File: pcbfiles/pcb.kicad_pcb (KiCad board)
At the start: 2 copper layers, 269.9 x 139.7 mm, 256 parts, among them J1 Conn_01x06, J2 Conn_01x06, J3 Conn_01x06, J4 Conn_01x06, J5 Conn_01x04_Female, J6 Conn_01x04_Female, Q1 AO3401A, Q2 AO3401A, SW1 SW_SPST, SW10 SW_SPST, SW11 SW_SPST, SW12 SW_SPST, SW13 SW_SPST, SW14 SW_SPST, SW15 SW_SPST, SW16 SW_SPST, SW17 SW_SPST, SW18 SW_SPST, SW19 SW_SPST, SW2 SW_SPST, SW20 SW_SPST, SW21 SW_SPST, SW22 SW_SPST, SW23 SW_SPST, SW24 SW_SPST, SW25 SW_SPST, SW26 SW_SPST, SW27 SW_SPST, SW28 SW_SPST, SW29 SW_SPST, SW3 SW_SPST, SW30 SW_SPST, SW31 SW_SPST, SW32 SW_SPST, SW33 SW_SPST, SW34 SW_SPST, SW35 SW_SPST, SW36 SW_SPST, SW37 SW_SPST, SW38 SW_SPST, SW39 SW_SPST, SW4 SW_SPST, SW40 SW_SPST, SW41 SW_SPST, SW42 SW_SPST, SW43 SW_SPST, SW44 SW_SPST, SW45 SW_SPST, SW46 SW_SPST, SW47 SW_SPST, SW48 SW_SPST, SW49 SW_SPST, SW5 SW_SPST, SW50 SW_SPST, SW51 SW_SPST, SW52 SW_SPST, SW53 SW_SPST, SW54 SW_SPST, SW55 SW_SPST, SW56 SW_SPST, SW57 SW_SPST, SW58 SW_SPST, SW59 SW_SPST, SW6 SW_SPST, SW60 SW_SPST, SW61 SW_SPST, SW62 SW_SPST, SW63 SW_SPST, SW64 SW_SPST, SW65 SW_SPST, SW66 SW_SPST, SW67 SW_SPST, SW68 SW_SPST, SW69 SW_SPST, SW7 SW_SPST, SW70 SW_SPST, SW71 SW_SPST, SW72 SW_SPST, SW73 SW_SPST, SW74 SW_SPST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

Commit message: Incremental routing
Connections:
- U5 pad 13: unconnected-(U5-Pad13) -> LH_ROW3
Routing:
- net VBUS: track 14.6 -> 65.3 mm, vias 0 -> 2
- net DBA_P2: track 10.9 -> 42.8 mm
- net LH_ROW2: track 124.9 -> 148.4 mm, vias 0 -> 2
- net VDD_NRF: track 2.25 -> 15.1 mm
- net RESET: track 0.00 -> 6.55 mm
- net LH_ROW3: track 107.4 -> 111.9 mm
- net DBA_P1: track 44.8 -> 42.7 mm
- net DBA_P5: track 44.7 -> 43.3 mm
- net unconnected-(U5-Pad4): track 1.10 -> 0.00 mm
- net unconnected-(U5-Pad3): track 1.10 -> 0.00 mm
- net unconnected-(U5-Pad2): track 1.10 -> 0.00 mm
- net DBA_P4: track 43.9 -> 43.2 mm
- net LH_COL0: vias 5 -> 7

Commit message: routing
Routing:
- net D-: track 5.70 -> 84.9 mm
- net D+: track 12.1 -> 82.8 mm
- net VBUS: track 65.3 -> 56.9 mm
- net LH_ROW2: vias 2 -> 4
- net LH_ROW3: vias 0 -> 2

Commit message: routing
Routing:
- net D+: track 82.8 -> 126.8 mm
- net VBUS: track 56.9 -> 16.0 mm, vias 2 -> 1
- net D-: track 84.9 -> 125.6 mm
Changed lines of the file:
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@@
   (arc (start 160.115395 69.557107) (mid 159.790972 69.77388) (end 159.408288 69.85) (width 0.25) (layer "B.Cu") (net 8))
   (arc (start 158.526714 69.85) (mid 158.144031 69.92612) (end 157.819607 70.142893) (width 0.25) (layer "B.Cu") (net 8))
-  (segment (start 7.9375 66.05) (end 7.9375 26.9875) (width 0.35) (layer "F.Cu") (net 9))
-  (via (at 7.9375 66.05) (size 0.8) (drill 0.4) (layers "F.Cu" "B.Cu") (net 9))
   (via (at 7.9375 26.9875) (size 0.8) (drill 0.4) (layers "F.Cu" "B.Cu") (net 9))
   (segment (start 79.375 68.675) (end 79.375 69.8) (width 0.35) (layer "B.Cu") (net 9))
@@
   (segment (start 7.9375 25.5875) (end 7.9375 26.9875) (width 0.35) (layer "B.Cu") (net 9))
   (segment (start 83.39375 67.675) (end 85.579536 67.675) (width 0.35) (layer "B.Cu") (net 9))
-  (segment (start 9.75 66.05) (end 7.9375 66.05) (width 0.35) (layer "B.Cu") (net 9))
   (segment (start 10.31875 26.075) (end 8.425 26.075) (width 0.35) (layer "B.Cu") (net 9))
   (arc (start 79.375 68.675) (mid 79.667893 67.967893) (end 80.375 67.675) (width 0.35) (layer "B.Cu") (net 9))
@@
   (arc (start -2.972895 29.592893) (mid -2.648472 29.37612) (end -2.265788 29.3) (width 0.35) (layer "B.Cu") (net 47))
   (arc (start -3.028554 33.851448) (mid -3.190766 33.743062) (end -3.382107 33.705002) (width 0.35) (layer "B.Cu") (net 47))
-  (segment (start 1.08125 31) (end 1.43125 30.65) (width 0.2) (layer "B.Cu") (net 48))
-  (segment (start 1.43125 30.65) (end 1.43125 30.75) (width 0.2) (layer "B.Cu") (net 48))
+  (segment (start 46.4 31.75) (end 2.43125 31.75) (width 0.2) (layer "B.Cu") (net 48))
+  (segment (start 1.091249 31.000001) (end 1.441249 30.650001) (width 0.2) (layer "B.Cu") (net 48))
   (segment (start 45.75 68.25) (end 9.75 68.25) (width 0.2) (layer "B.Cu") (net 48))
-  (segment (start -2.5 32) (end -1.33 32) (width 0.2) (layer "B.Cu") (net 48))
+  (segment (start -2.990001 31.500001) (end -2.990001 31.500001) (width 0.2) (layer "B.Cu") (net 48))
+  (segment (start 1.441249 30.650001) (end 1.441249 30.750001) (width 0.2) (layer "B.Cu") (net 48))
+  (segment (start -2.490001 31.000001) (end -1.320001 31.000001) (width 0.2) (layer "B.Cu") (net 48))
   (segment (start 47.85 33.2) (end 47.85 66.15) (width 0.2) (layer "B.Cu") (net 48))
-  (segment (start -1.33 31) (end 1.08125 31) (width 0.2) (layer "B.Cu") (net 48))
-  (segment (start -3 31.5) (end -3 31.5) (width 0.2) (layer "B.Cu") (net 48))
-  (segment (start -2.5 31) (end -1.33 31) (width 0.2) (layer "B.Cu") (net 48))
-  (arc (start -2.5 31) (mid -2.853553 31.146447) (end -3 31.5) (width 0.2) (layer "B.Cu") (net 48))
+  (segment (start -2.490001 32.000001) (end -1.320001 32.000001) (width 0.2) (layer "B.Cu") (net 48))
+  (segment (start -1.320001 31.000001) (end 1.091249 31.000001) (width 0.2) (layer "B.Cu") (net 48))
   (arc (start 1.43125 30.75) (mid 1.724143 31.457107) (end 2.43125 31.75) (width 0.2) (layer "B.Cu") (net 48))
+  (arc (start -2.490001 32.000001) (mid -2.843554 31.853554) (end -2.990001 31.500001) (width 0.2) (layer "B.Cu") (net 48))
   (arc (start 45.75 68.25) (mid 47.234924 67.634924) (end 47.85 66.15) (width 0.2) (layer "B.Cu") (net 48))
-  (arc (start -2.5 32) (mid -2.853553 31.853553) (end -3 31.5) (width 0.2) (layer "B.Cu") (net 48))
+  (arc (start -2.490001 31.000001) (mid -2.843554 31.146448) (end -2.990001 31.500001) (width 0.2) (layer "B.Cu") (net 48))
   (arc (start 46.4 31.75) (mid 47.425305 32.174695) (end 47.85 33.2) (width 0.2) (layer "B.Cu") (net 48))
-  (segment (start -1.33 31.5) (end -0.16 31.5) (width 0.2) (layer "B.Cu") (net 49))
-  (segment (start 9.75 67.15) (end 46.4 67.15) (width 0.2) (layer "B.Cu") (net 49))
+  (segment (start -1.320001 32.500001) (end -0.150001 32.500001) (width 0.2) (layer "B.Cu") (net 49))
+  (segment (start 1.091249 32.500001) (end 0.849999 32.500001) (width 0.2) (layer "B.Cu") (net 49))
+  (segment (start 11.548882 67.698883) (end 11.6 67.698883) (width 0.2) (layer "B.Cu") (net 49))
+  (segment (start 46.4 32.2) (end 4.8 32.2) (width 0.2) (layer "B.Cu") (net 49))
+  (segment (start 1.43125 32.85) (end 1.08125 32.5) (width 0.2) (layer "B.Cu") (net 49))
+  (segment (start 0.349999 32.000001) (end 0.349999 32.000001) (width 0.2) (layer "B.Cu") (net 49))
+  (segment (start 4.3 32.7) (end 4.3 33.35) (width 0.2) (layer "B.Cu") (net 49))
+  (segment (start 1.43125 32.85) (end 1.43125 32.85) (width 0.2) (layer "B.Cu") (net 49))
+  (segment (start 0.349999 32.000001) (end 0.349999 32.000001) (width 0.2) (layer "B.Cu") (net 49))
+  (segment (start 12.148882 67.15) (end 12.2 67.15) (width 0.2) (layer "B.Cu") (net 49))
   (segment (start 3.8 33.85) (end 2.43125 33.85) (width 0.2) (layer "B.Cu") (net 49))
-  (segment (start -1.33 32.5) (end -0.16 32.5) (width 0.2) (layer "B.Cu") (net 49))
-  (segment (start 4.3 33.35) (end 4.3 32.7) (width 0.2) (layer "B.Cu") (net 49))
-  (segment (start 1.43125 32.85) (end 1.08125 32.5) (width 0.2) (layer "B.Cu") (net 49))
-  (segment (start 1.43125 32.85) (end 1.43125 32.85) (width 0.2) (layer "B.Cu") (net 49))
+  (segment (start 11.874441 67.424442) (end 11.874441 67.424441) (width 0.2) (layer "B.Cu") (net 49))
+  (segment (start 12.2 67.15) (end 46.4 67.15) (width 0.2) (layer "B.Cu") (net 49))
+  (segment (start 1.43125 32.85) (end 1.43125 33.18125) (width 0.2) (layer "B.Cu") (net 49))
+  (segment (start 11.274441 67.424441) (end 11.274441 67.424442) (width 0.2) (layer "B.Cu") (net 49))
   (segment (start 47.4 66.15) (end 47.4 33.2) (width 0.2) (layer "B.Cu") (net 49))
-  (segment (start 1.08125 32.5) (end 0.84 32.5) (width 0.2) (layer "B.Cu") (net 49))
-  (segment (start 0.34 32) (end 0.34 32) (width 0.2) (layer "B.Cu") (net 49))
-  (segment (start 4.8 32.2) (end 6.3 32.2) (width 0.2) (layer "B.Cu") (net 49))
-  (segment (start 0.34 32) (end 0.34 32) (width 0.2) (layer "B.Cu") (net 49))
-  (segment (start 1.43125 32.85) (end 1.43125 33.18125) (width 0.2) (layer "B.Cu") (net 49))
-  (arc (start 0.34 32) (mid 0.193553 31.646447) (end -0.16 31.5) (width 0.2) (layer "B.Cu") (net 49))
+  (segment (start 9.75 67.15) (end 11 67.15) (width 0.2) (layer "B.Cu") (net 49))
+  (segment (start -1.320001 31.500001) (end -0.150001 31.500001) (width 0.2) (layer "B.Cu") (net 49))
+  (arc (start -0.150001 32.500001) (mid 0.203552 32.353554) (end 0.349999 32.000001) (width 0.2) (layer "B.Cu") (net 49))
+  (arc (start 2.43125 33.85) (mid 1.724143 33.557107) (end 1.43125 32.85) (width 0.2) (layer "B.Cu") (net 49))
+  (arc (start 11.874441 67.424441) (mid 11.954823 67.230382) (end 12.148882 67.15) (width 0.2) (layer "B.Cu") (net 49))
+  (arc (start 11 67.15) (mid 11.194059 67.230382) (end 11.274441 67.424441) (width 0.2) (layer "B.Cu") (net 49))
+  (arc (start 46.4 67.15) (mid 47.107107 66.857107) (end 47.4 66.15) (width 0.2) (layer "B.Cu") (net 49))
+  (arc (start 0.349999 32.000001) (mid 0.203552 31.646448) (end -0.150001 31.500001) (width 0.2) (layer "B.Cu") (net 49))
+  (arc (start 11.6 67.698883) (mid 11.794059 67.618501) (end 11.874441 67.424442) (width 0.2) (layer "B.Cu") (net 49))
+  (arc (start 4.8 32.2) (mid 4.446447 32.346447) (end 4.3 32.7) (width 0.2) (layer "B.Cu") (net 49))
+  (arc (start 4.3 33.35) (mid 4.153553 33.703553) (end 3.8 33.85) (width 0.2) (layer "B.Cu") (net 49))
   (arc (start 47.4 33.2) (mid 47.107107 32.492893) (end 46.4 32.2) (width 0.2) (layer "B.Cu") (net 49))
-  (arc (start 4.3 32.7) (mid 4.446447 32.346447) (end 4.8 32.2) (width 0.2) (layer "B.Cu") (net 49))
-  (arc (start -0.16 32.5) (mid 0.193553 32.353553) (end 0.34 32) (width 0.2) (layer "B.Cu") (net 49))
-  (arc (start 0.34 32) (mid 0.486447 32.353553) (end 0.84 32.5) (width 0.2) (layer "B.Cu") (net 49))
-  (arc (start 2.43125 33.85) (mid 1.724143 33.557107) (end 1.43125 32.85) (width 0.2) (layer "B.Cu") (net 49))
-  (arc (start 3.8 33.85) (mid 4.153553 33.703553) (end 4.3 33.35) (width 0.2) (layer "B.Cu") (net 49))
-  (arc (start 47.4 66.15) (mid 47.107107 66.857107) (end 46.4 67.15) (width 0.2) (layer "B.Cu") (net 49))
+  (arc (start 0.349999 32.000001) (mid 0.496446 32.353554) (end 0.849999 32.500001) (width 0.2) (layer "B.Cu") (net 49))
+  (arc (start 11.274441 67.424442) (mid 11.354823 67.618501) (end 11.548882 67.698883) (width 0.2) (layer "B.Cu") (net 49))
   (segment (start 246.5705 43.18) (end 246.5705 40.75) (width 0.25) (layer "B.Cu") (net 50))
   (segment (start 249.2375 39.75) (end 247.5705 39.75) (width 0.25) (layer "B.Cu") (net 50))
@@
   (via (at -7.14375 42.06875) (size 0.8) (drill 0.4) (layers "F.Cu" "B.Cu") (net 105))
   (arc (start -4.7625 41.06875) (mid -5.055393 41.775857) (end -5.7625 42.06875) (width 0.25) (layer "F.Cu") (net 105))
+  (segment (start -3.455776 32.707108) (end -3.472687 32.690197) (width 0.25) (layer "B.Cu") (net 105))
   (segment (start -1.33 33) (end -2.758668 33) (width 0.25) (layer "B.Cu") (net 105))
   (segment (start -4.7625 32.54375) (end -3.836239 32.54375) (width 0.25) (layer "B.Cu") (net 105))
-  (segment (start -3.465775 32.707107) (end -3.482686 32.690196) (width 0.25) (layer "B.Cu") (net 105))
   (segment (start -7.14375 43.5375) (end -7.14375 42.06875) (width 0.25) (layer "B.Cu") (net 105))
   (arc (start -2.758668 33) (mid -3.141351 32.92388) (end -3.465775 32.707107) (width 0.25) (layer "B.Cu") (net 105))

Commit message: Today's minor progress
I had a short break from responsibilities today, and made some progress. Discord wants to update and I'm data limited, so I can't message you right now, but I'm happy with my progress and appreciate your flexibility on deadline.
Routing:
- net RESET: track 6.55 -> 112.8 mm, vias 0 -> 2
- net BVOLT: track 2.38 -> 105.1 mm, vias 0 -> 4
- net VDD_NRF: track 15.1 -> 98.3 mm, vias 0 -> 2
- net Net-(D94-Pad1): track 3.98 -> 14.4 mm
- net VBAT: track 24.0 -> 27.7 mm
- net Net-(C5-Pad1): track 12.2 -> 8.79 mm

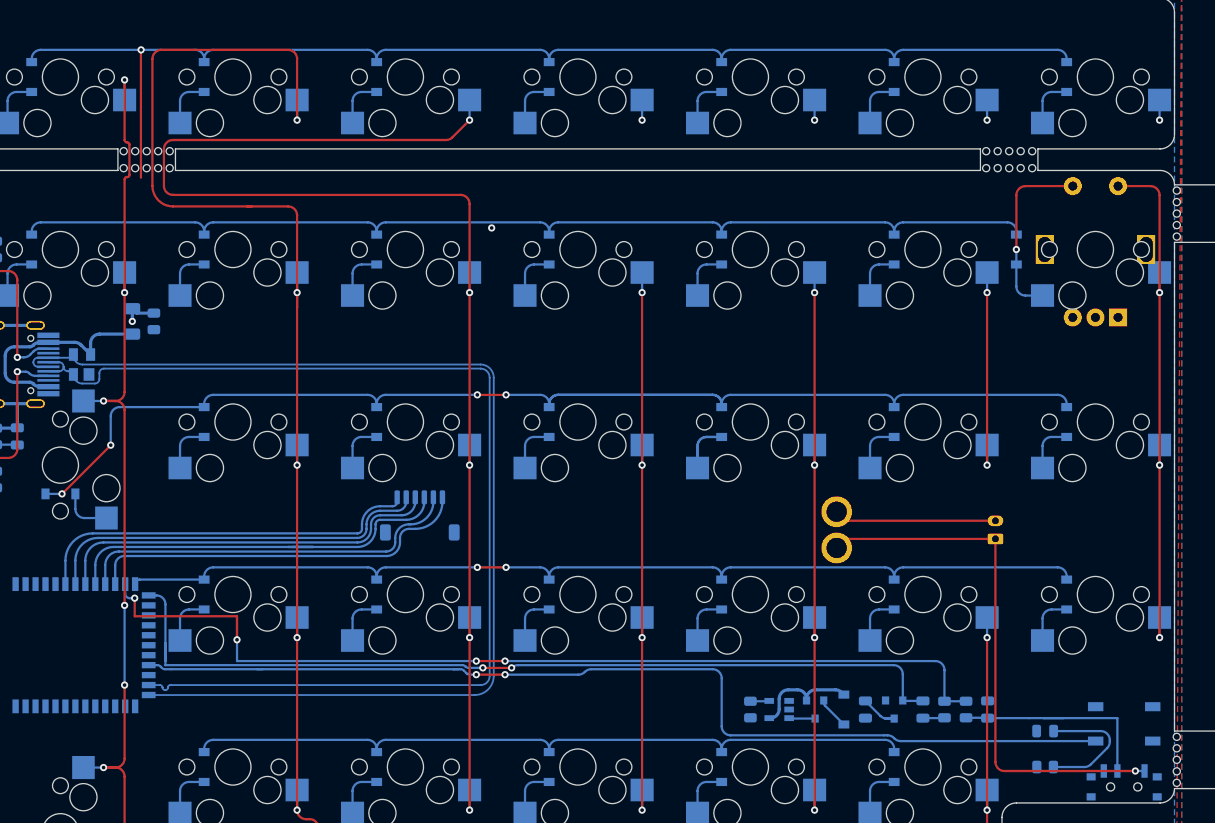
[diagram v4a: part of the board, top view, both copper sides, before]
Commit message: Routing for the left half.
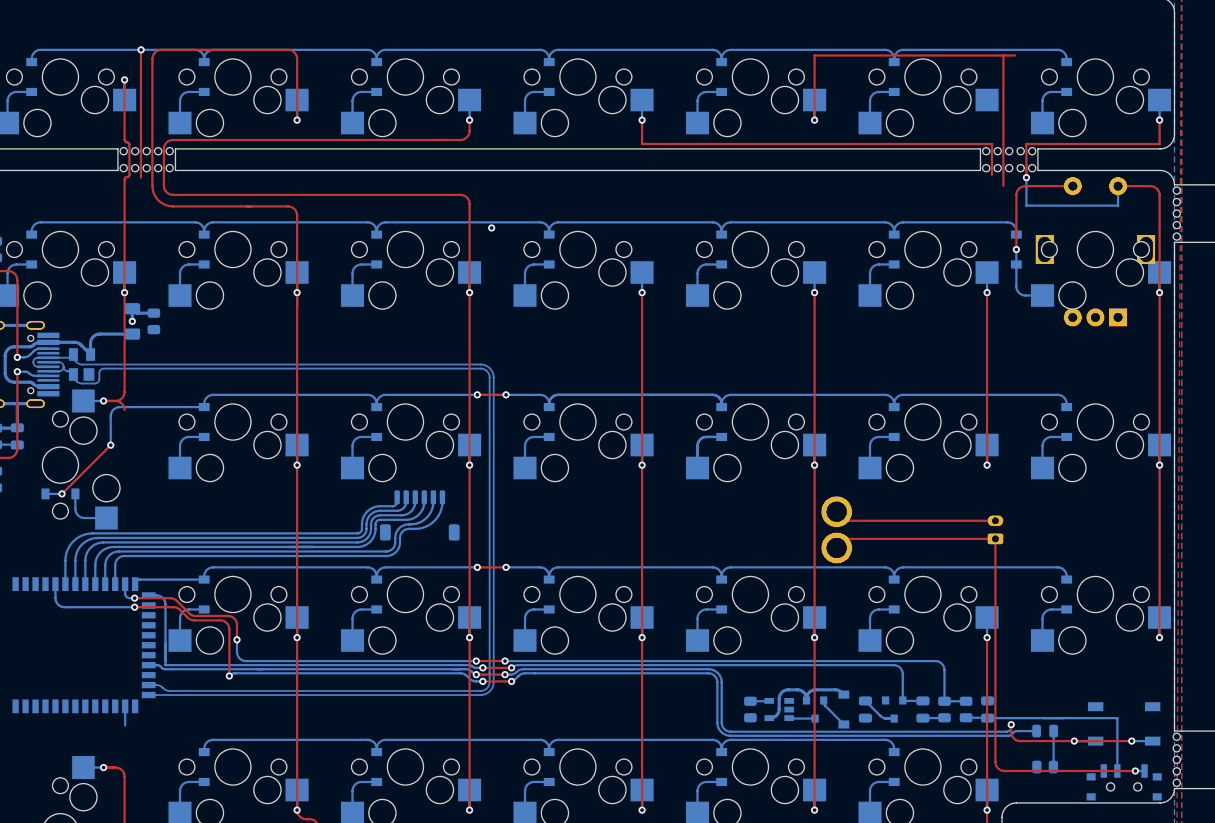
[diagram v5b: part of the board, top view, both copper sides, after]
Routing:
- net LED_1: track 0.00 -> 123.2 mm, vias 0 -> 4
- net LH_COL3: track 68.3 -> 112.9 mm
- net LH_COL4: track 68.3 -> 111.9 mm
- net LH_COL0: track 130.3 -> 90.3 mm, vias 7 -> 5
- net ENC_P1: track 62.9 -> 99.3 mm, vias 4 -> 5
- net Net-(D94-Pad1): track 14.4 -> 3.98 mm
- net RESET: track 112.8 -> 122.9 mm, vias 2 -> 5
- net LH_COL5: track 70.5 -> 68.3 mm, vias 6 -> 5
- net BVOLT: track 105.1 -> 102.9 mm
- net unconnected-(U5-Pad26): track 0.00 -> 2.10 mm
- net LH_COL2: track 152.1 -> 153.9 mm
- net D-: track 125.6 -> 126.2 mm

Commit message: Routing progress.
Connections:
- U5 pad 2: unconnected-(U5-Pad2) -> LH_ROW1
- U5 pad 3: unconnected-(U5-Pad3) -> LH_ROW0
- U5 pad 4: unconnected-(U5-Pad4) -> LH_ROW2
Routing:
- net DBA_P2: track 42.8 -> 154.6 mm, vias 0 -> 2
- net LH_ROW5: track 0.00 -> 91.8 mm
- net DBA_P5: track 43.3 -> 128.8 mm, vias 0 -> 2
- net DBA_P4: track 43.2 -> 118.2 mm, vias 0 -> 2
- net DBA_P3: track 47.9 -> 119.7 mm, vias 0 -> 2
- net DBA_P6: track 43.4 -> 114.9 mm, vias 0 -> 2
- net DBA_P1: track 42.7 -> 110.0 mm, vias 0 -> 2
- net LH_ROW0: track 139.0 -> 193.5 mm, vias 1 -> 2
- net unconnected-(U5-Pad30): track 0.00 -> 53.4 mm
- net LH_COL0: track 90.3 -> 140.2 mm, vias 5 -> 6
- net unconnected-(U5-Pad29): track 0.00 -> 48.6 mm
- net unconnected-(U5-Pad28): track 0.00 -> 47.4 mm
- net unconnected-(U5-Pad27): track 0.00 -> 46.0 mm
- net unconnected-(U5-Pad26): track 2.10 -> 44.7 mm
- net LH_ROW1: track 119.3 -> 160.7 mm, vias 0 -> 2
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
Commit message: practically done with the left half
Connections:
- U5 pad 26: unconnected-(U5-Pad26) -> LH_COL5
- U5 pad 27: unconnected-(U5-Pad27) -> LH_COL4
- U5 pad 28: unconnected-(U5-Pad28) -> LH_COL3
- U5 pad 29: unconnected-(U5-Pad29) -> LH_COL2
- U5 pad 30: unconnected-(U5-Pad30) -> LH_COL1
- U5 pad 33: unconnected-(U5-Pad33) -> LH_COL0
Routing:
- net LH_COL5: track 68.3 -> 168.8 mm, vias 5 -> 6
- net LH_COL4: track 111.9 -> 199.0 mm, vias 5 -> 6
- net LH_COL3: track 112.9 -> 179.1 mm, vias 5 -> 6
- net unconnected-(U5-Pad30): track 53.4 -> 0.00 mm
- net unconnected-(U5-Pad29): track 48.6 -> 0.00 mm
- net LH_COL2: track 153.9 -> 202.1 mm, vias 5 -> 6
- net unconnected-(U5-Pad28): track 47.4 -> 0.00 mm
- net unconnected-(U5-Pad27): track 46.0 -> 0.00 mm
- net unconnected-(U5-Pad26): track 44.7 -> 0.00 mm
- net LH_COL0: track 140.2 -> 179.1 mm
- net LH_COL1: track 157.2 -> 187.3 mm, vias 6 -> 7
- net LH_ROW2: track 158.3 -> 163.8 mm
- net SWD: track 0.00 -> 1.60 mm, vias 0 -> 1
- net SWC: track 0.00 -> 1.60 mm, vias 0 -> 1

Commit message: Routing.
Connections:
- U5 pad 15: unconnected-(U5-Pad15) -> ENC_P1
- U5 pad 16: unconnected-(U5-Pad16) -> ENC_A
- U5 pad 17: unconnected-(U5-Pad17) -> ENC_B
- U5 pad 35: unconnected-(U5-Pad35) -> LH_ROW4
- U5 pad 36: unconnected-(U5-Pad36) -> LH_ROW5
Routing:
- net VBUS: track 16.0 -> 93.3 mm, vias 1 -> 2
- net LH_ROW5: track 91.8 -> 166.2 mm
- net LH_ROW4: track 83.2 -> 141.0 mm
- net SWC: track 1.60 -> 58.3 mm
- net SWD: track 1.60 -> 54.7 mm
- net Net-(D75-Pad2): track 5.63 -> 0.00 mm
- net DBA_ROW0: track 0.00 -> 5.63 mm
- net VDD_NRF: track 98.3 -> 97.4 mm
- net LH_ROW0: track 193.5 -> 192.8 mm
- net RESET: track 122.9 -> 122.2 mm
